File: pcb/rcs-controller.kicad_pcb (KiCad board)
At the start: 2 copper layers, 100 x 75 mm, 86 parts, among them J1 00222-32051, J10 0022-232021, J2 0022-232021, J3 0022-232041, J4 Screw_Terminal_4_P3.50mm, J8 00222-32051, Q1 SI7465DP-T1-E3, Q2 SI7465DP-T1-E3, Q3 SI7465DP-T1-E3, Q4 PMV45EN2, Q5 PMV45EN2, U1 LSM6DSOX, U2 MP26123DR-LF-Z, U3 TPS63070, U4 FeatherS3

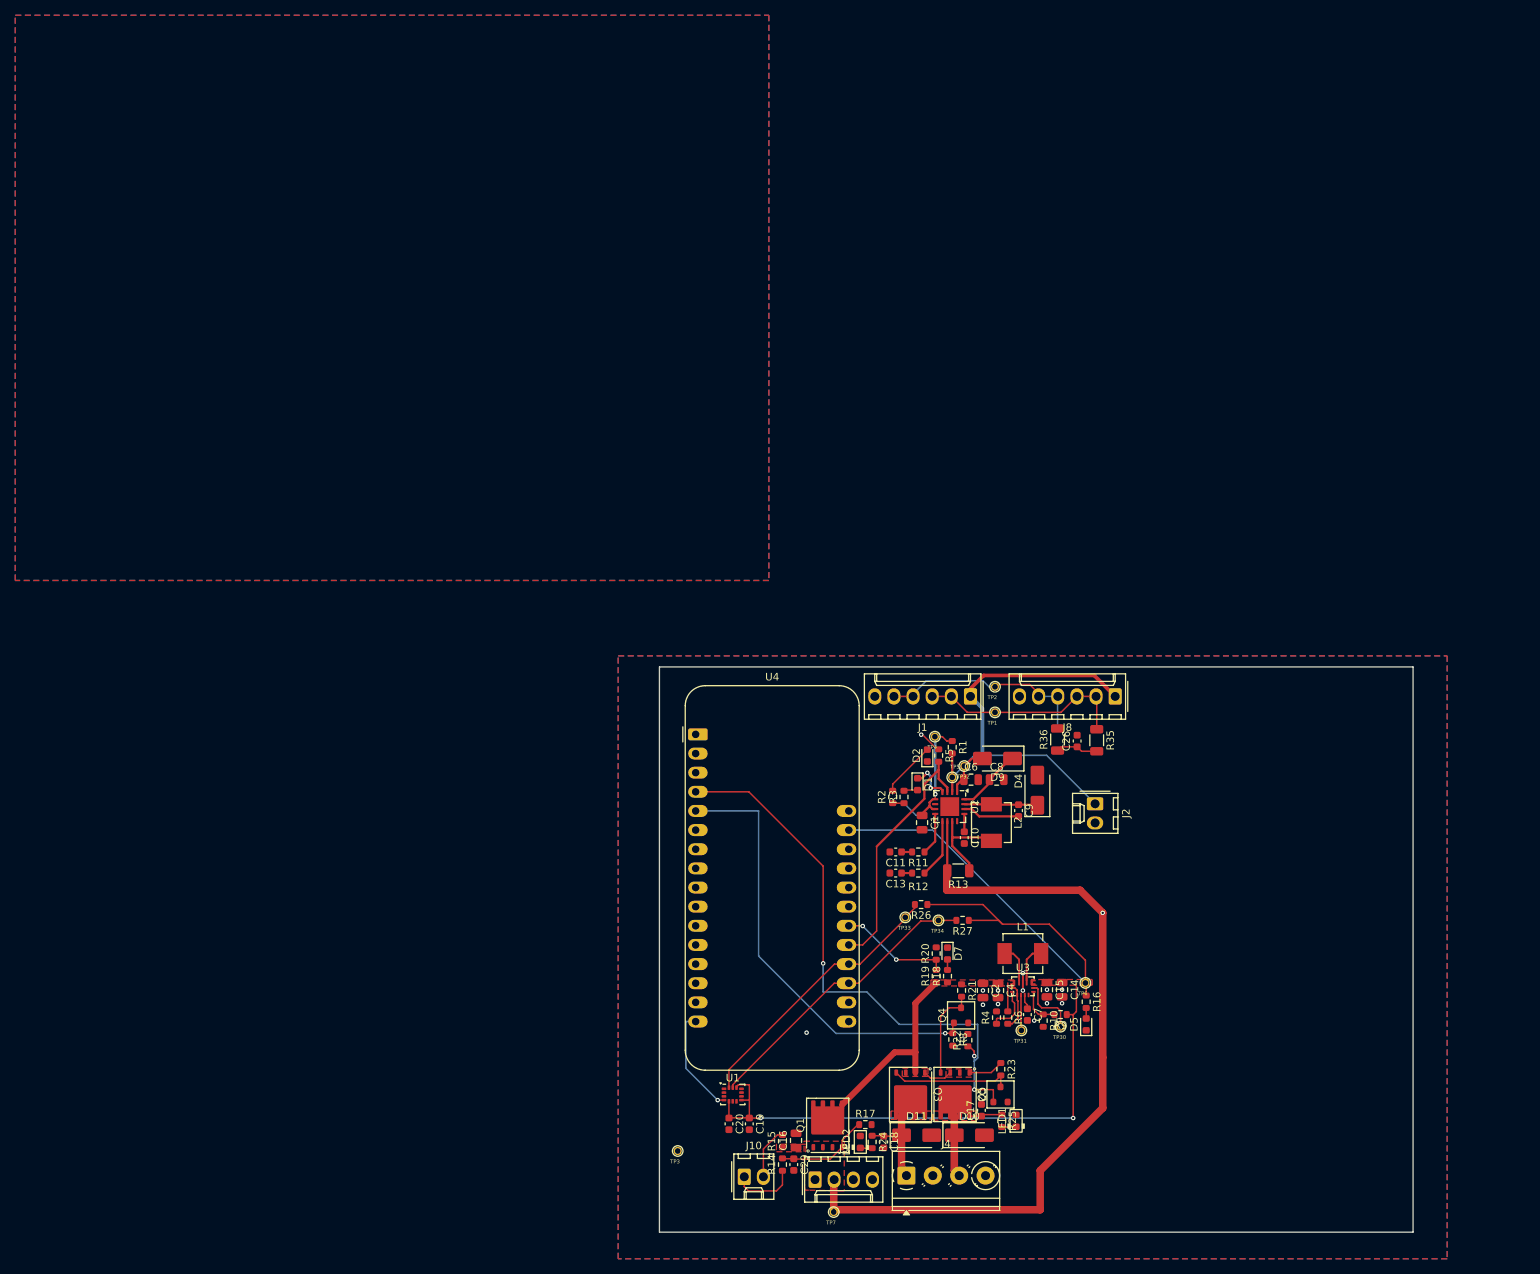
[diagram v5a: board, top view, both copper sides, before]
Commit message: Cleanup of Jacob's board; mostly ready for fab
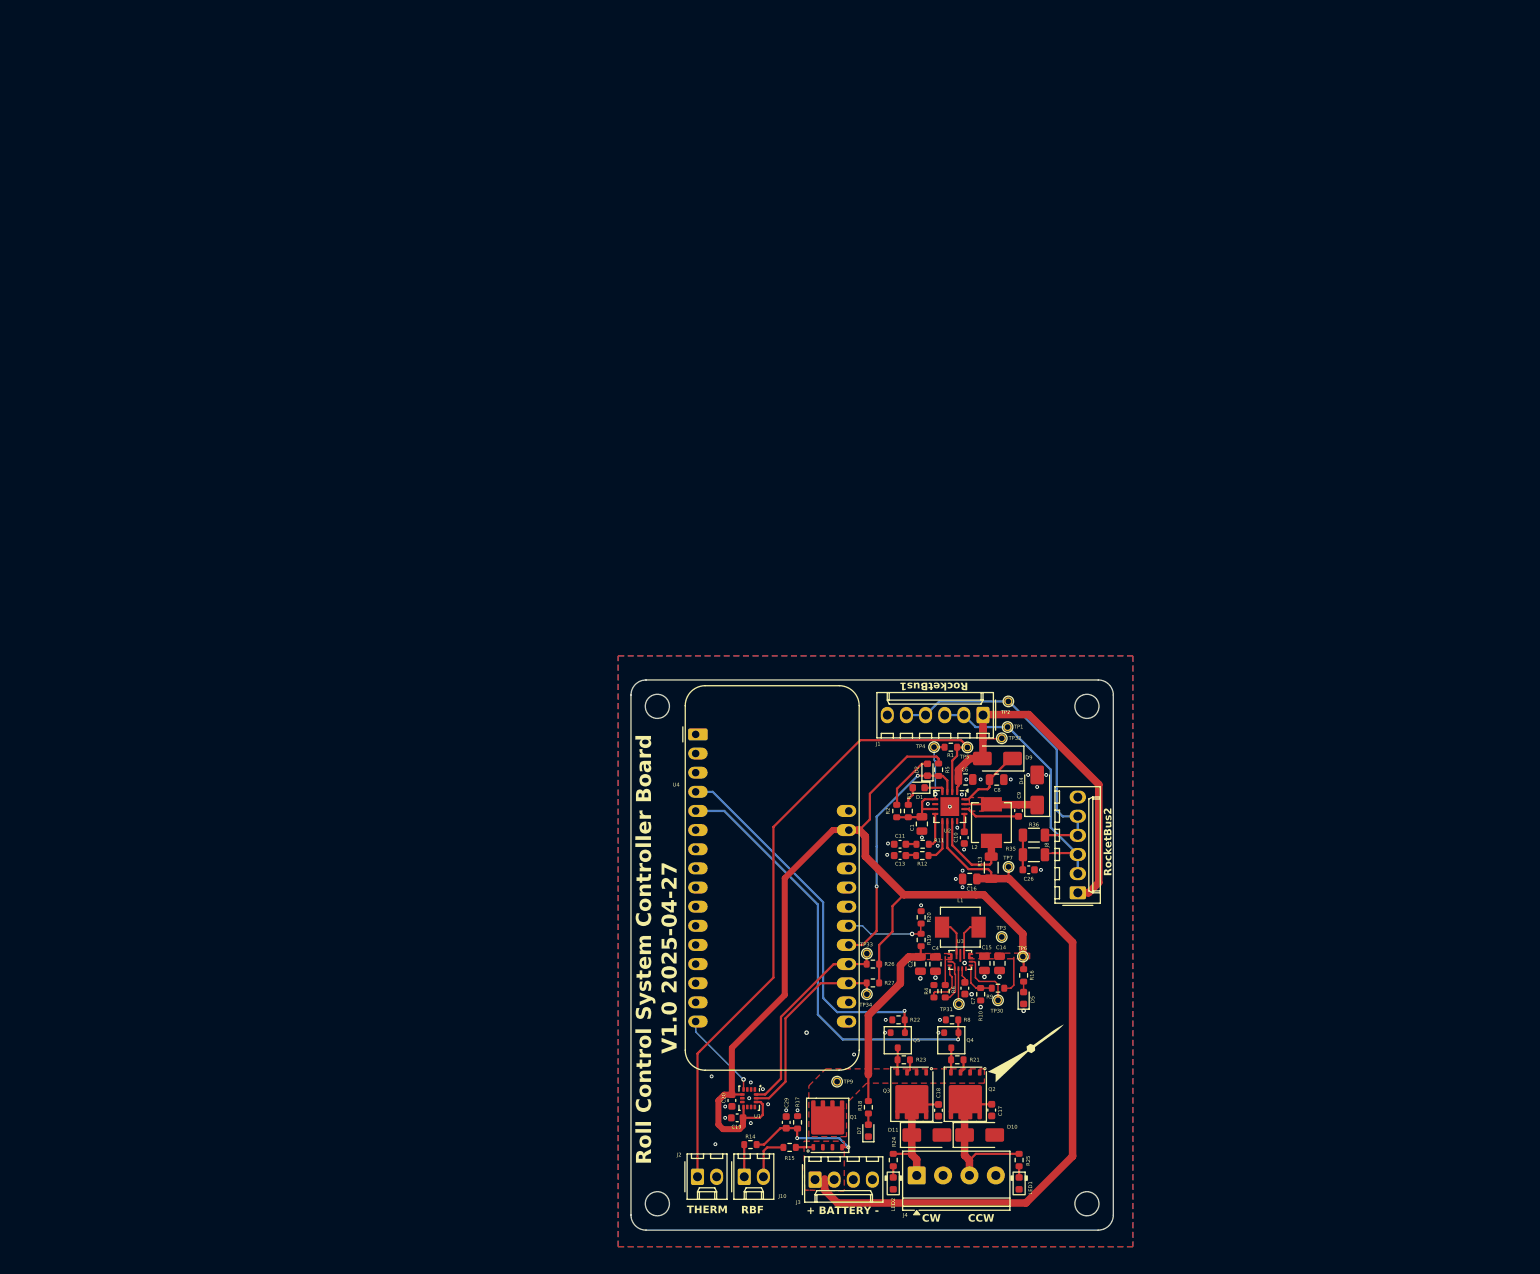
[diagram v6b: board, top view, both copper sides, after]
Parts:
- added LOGO1: , psas-graphics:PSAS_LOGO_10X10, F.Cu at (134.4, 127.4)
- added REF**: MountingHole_3.2mm_M3, MountingHole:MountingHole_3.2mm_M3, F.Cu at (142.2, 81.7)
- added REF**: MountingHole_3.2mm_M3, MountingHole:MountingHole_3.2mm_M3, F.Cu at (85.2, 81.7)
- added REF**: MountingHole_3.2mm_M3, MountingHole:MountingHole_3.2mm_M3, F.Cu at (142.2, 147.7)
- added REF**: MountingHole_3.2mm_M3, MountingHole:MountingHole_3.2mm_M3, F.Cu at (85.2, 147.7)
- added TP9: Test-Point, psas-footprints:TP-through-hole-1X01, F.Cu at (109.0, 131.5)
- moved J2 72.3 mm to (90.5, 144.1), turned to 0 degrees
- moved TP3 51.5 mm to (130.9, 112.3)
- moved TP7 51.3 mm to (131.8, 103.0)
- moved C16 41.7 mm to (126.7, 104.6), turned to 180 degrees
- moved J8 26.5 mm to (141.0, 106.4), turned to 90 degrees
- moved D7 25.7 mm to (113.2, 138.0), turned to 90 degrees
- moved R18 20.3 mm to (113.2, 134.9), turned to -90 degrees
- moved C26 18.3 mm to (134.5, 103.4), turned to 0 degrees
- moved R35 17.3 mm to (135.2, 101.4), turned to 180 degrees
- moved Q5 15.4 mm to (117.1, 126.0), turned to -90 degrees
- moved R27 14.5 mm to (113.8, 118.4)
- moved TP34 13.6 mm to (113.0, 119.9)
- moved R36 13.1 mm to (135.2, 98.8), turned to 0 degrees
- moved R23 12.9 mm to (117.9, 128.6), turned to 180 degrees
- moved R26 10.2 mm to (113.8, 115.9)
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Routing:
- net Net-(J2-Pin_1): track 27.9 -> 89.2 mm
- net Net-(Q5-G): track 75.9 -> 50.3 mm, vias 3 -> 1
- net +3.3V: track 151.9 -> 131.6 mm, vias 3 -> 0
- net CANL: track 28.4 -> 41.9 mm
- net /Power/VUMB: track 37.8 -> 50.8 mm
- net Net-(Q3-G): track 16.2 -> 3.29 mm
- net Net-(U1-SCL): track 39.1 -> 27.4 mm
- net CANH: track 27.9 -> 37.8 mm
- net Net-(Q2-G): track 12.2 -> 3.29 mm
- net Net-(U1-SDA): track 37.0 -> 28.3 mm
- net Net-(D10-K): track 12.7 -> 21.4 mm
- net +BATT: track 106.1 -> 98.6 mm, vias 2 -> 0
- net VBUS: track 38.2 -> 32.0 mm
- net /Power/ARM-IN: track 8.82 -> 4.27 mm
- net Net-(D11-K): track 13.3 -> 16.9 mm
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- added copper zone on F.Cu, net Net-(D4-K)
- removed copper zone on F.Cu, net (none)
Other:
- board size 100 x 75 mm -> 64 x 73 mm
- board text added: "+ BATTERY -"
- board text added: "CCW"
- board text added: "CW"
- board text added: "RBF"
- board text added: "RocketBus1"
- board text added: "RocketBus2"
- board text added: "Roll Control System Controller Board"
- board text added: "THERM"
- board text added: "V${REVISION} ${ISSUE_DATE}"

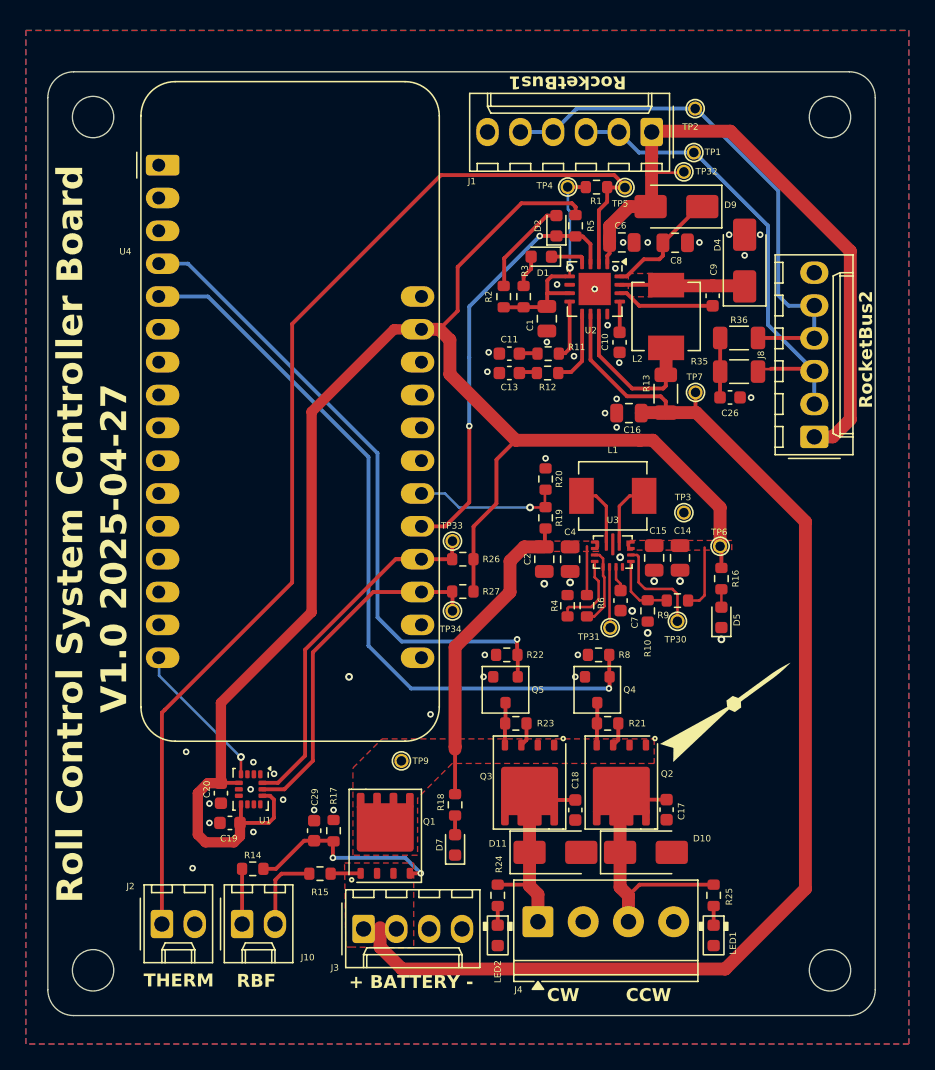
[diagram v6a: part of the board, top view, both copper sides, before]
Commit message: Fixed BOM, fixed missing symbol and footprint libraries, stitched vias, generated Gerbers.
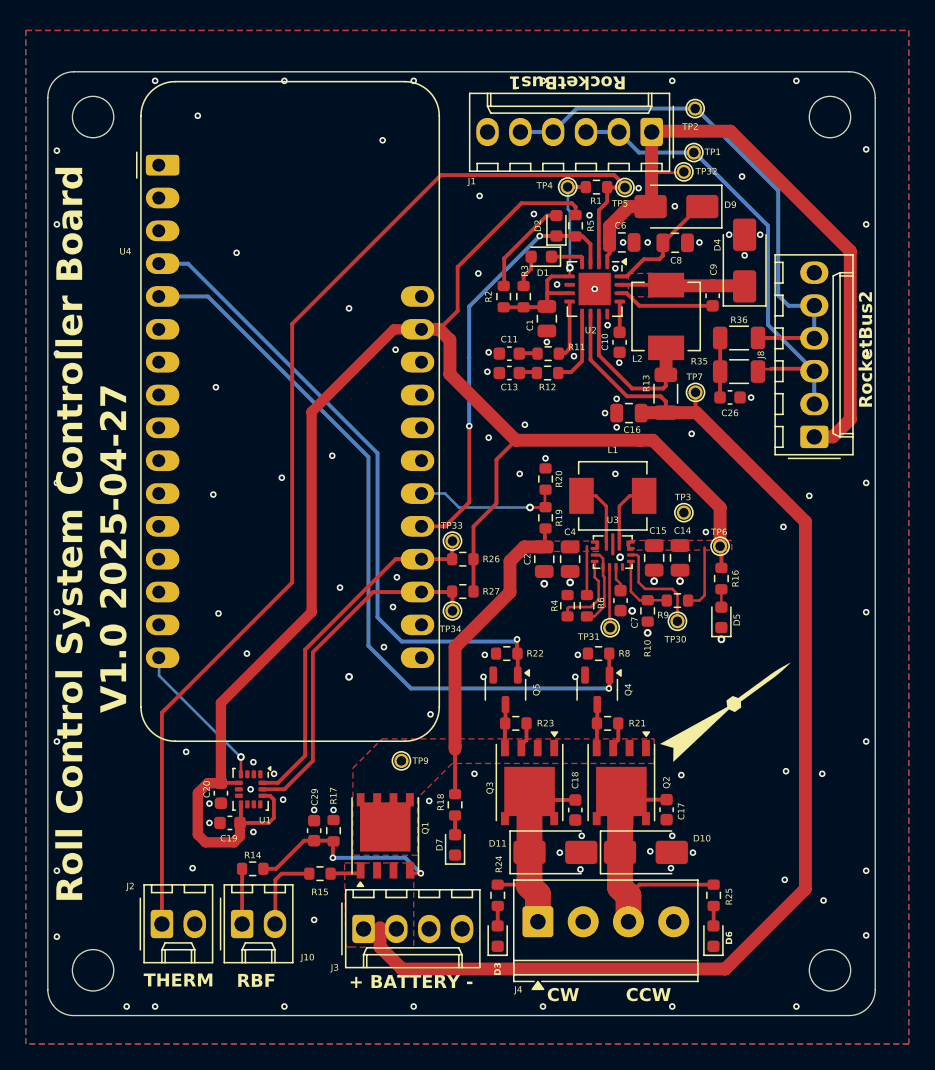
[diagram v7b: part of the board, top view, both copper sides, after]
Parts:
- removed LED1, LED2: LED_0603_Amber, PCM_LED_SMD_AKL:LED_0603_1608Metric
- added D3: Amber, LED_SMD:LED_0603_1608Metric, F.Cu at (116.5, 145.1)
- added D6: Amber, LED_SMD:LED_0603_1608Metric, F.Cu at (133.2, 145.1)
- Q1, Q2, Q3: footprint PCM_Package_SON_AKL:Infineon_PG-TDSON-8 -> Package_SO:PowerPAK_SO-8_Single
- Q4, Q5: footprint PCM_Package_TO_SOT_SMD_AKL:SOT-23 -> Package_TO_SOT_SMD:SOT-23-3
- moved R22 0.10 mm to (117.2, 123.2)
- moved R8 0.10 mm to (124.3, 123.2)
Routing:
- net GND: vias 45 -> 119

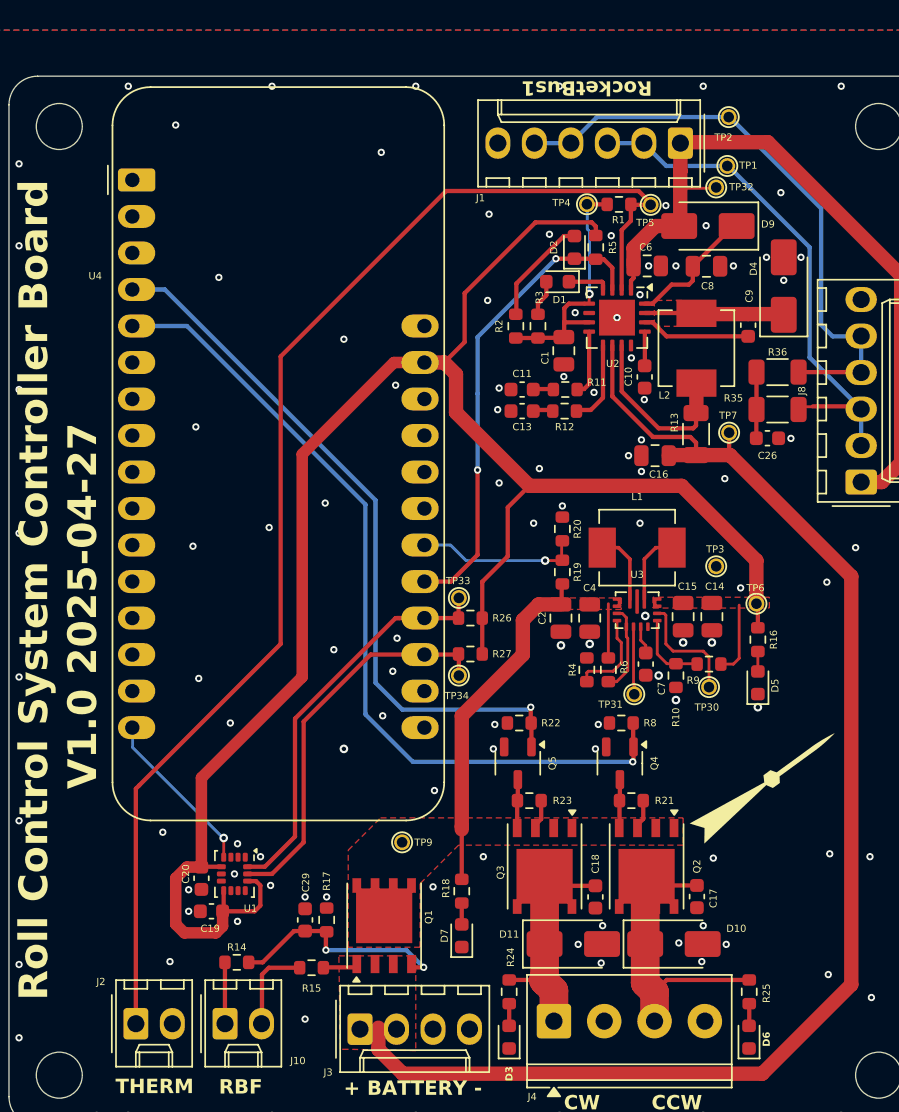
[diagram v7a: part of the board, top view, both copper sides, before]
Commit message: Rev 2.0
Updated board with ESP32 chip to replace feather
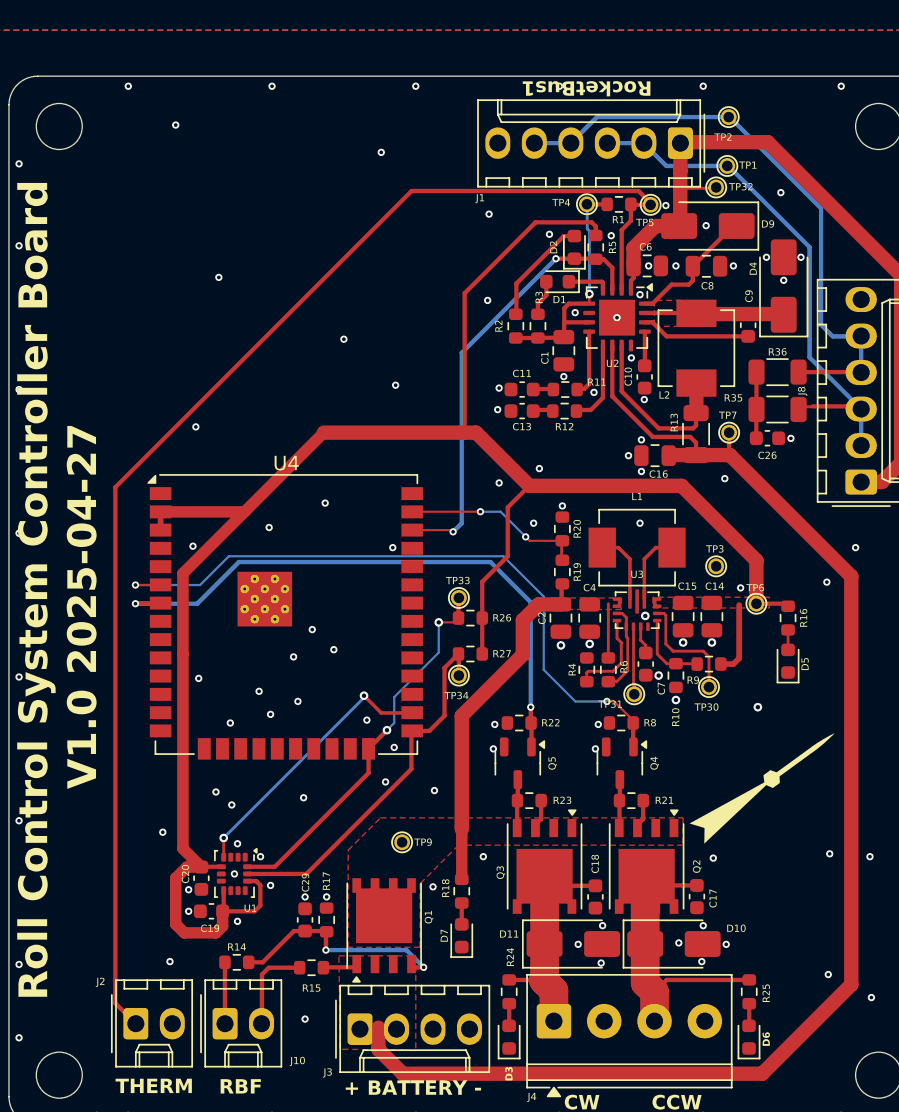
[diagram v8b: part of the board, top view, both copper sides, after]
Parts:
- U4: value FeatherS3 -> ESP32-WROOM-32UE; footprint Module:Adafruit_Feather -> RF_Module:ESP32-WROOM-32UE
- moved U4 32.1 mm to (101.0, 115.7)
- moved D5 2.58 mm to (135.9, 118.9)
- moved R16 2.58 mm to (135.9, 115.9)
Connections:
- R26 pad 2: Net-(U1-SDA) -> Net-(U1-CS)
- TP33 pad 1: Net-(U1-SDA) -> Net-(U1-CS)
- U1 pad 12: +3.3V -> Net-(U1-CS)
- U1 pad 14: Net-(U1-SDA) -> Net-(U1-CS)
- U4 pad 1: unconnected-(U4-VBAT-Pad1) -> GND
- U4 pad 15: unconnected-(U4-RX-Pad15) -> GND
- U4 pad 16: Net-(U1-INT1) -> unconnected-(U4-IO13-Pad16)
- U4 pad 19: Net-(U1-SCL) -> unconnected-(U4-NC-Pad19)
- U4 pad 2: unconnected-(U4-EN-Pad2) -> +3.3V
- U4 pad 20: Net-(U1-SDA) -> unconnected-(U4-NC-Pad20)
- U4 pad 21: UMB_~{ON} -> unconnected-(U4-NC-Pad21)
- U4 pad 22: BATT_READ -> unconnected-(U4-NC-Pad22)
- U4 pad 24: unconnected-(U4-IO17-Pad24) -> Net-(U1-CS)
- U4 pad 25: GND -> Net-(U1-SCL)
- U4 pad 26: unconnected-(U4-IO0-Pad26) -> Net-(U1-INT1)
- U4 pad 27: +3.3V -> unconnected-(U4-IO16-Pad27)
- U4 pad 3: unconnected-(U4-5V-Pad3) -> +3.3V
- U4 pad 4: Net-(Q5-G) -> unconnected-(U4-SENSOR_VP-Pad4)
- U4 pad 5: Net-(Q4-G) -> unconnected-(U4-SENSOR_VN-Pad5)
- U4 pad 6: unconnected-(U4-IO7-Pad6) -> Net-(Q4-G)
- U4 pad 7: unconnected-(U4-IO3-Pad7) -> Net-(Q5-G)
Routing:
- net Net-(U1-SDA): track 28.3 -> 0.00 mm
- net Net-(U1-CS): track 0.00 -> 26.4 mm, vias 0 -> 2
- net Net-(Q4-G): track 58.7 -> 46.8 mm, vias 1 -> 2
- net Net-(Q5-G): track 50.3 -> 41.8 mm, vias 1 -> 2
- net +3.3V: track 131.6 -> 139.3 mm
- net Net-(U1-INT1): track 11.7 -> 19.2 mm, vias 1 -> 2
- net Net-(J2-Pin_1): track 89.2 -> 91.8 mm
- net UMB_~{ON}: track 33.0 -> 30.6 mm
- net BATT_READ: track 11.9 -> 13.6 mm, vias 1 -> 2
- net Net-(U1-SCL): track 27.4 -> 26.0 mm
- net GND: vias 119 -> 127
